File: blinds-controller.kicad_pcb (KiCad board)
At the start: 2 copper layers, 50 x 70 mm, 18 parts, among them J1 Jack-DC, J2 Stepper Motor, J3 DC Check, J4 JTAG, SW1 RESET, U1 MPM3610AGQV-P, U2 ESP32-S2-WROOM, U3 ULN2003A

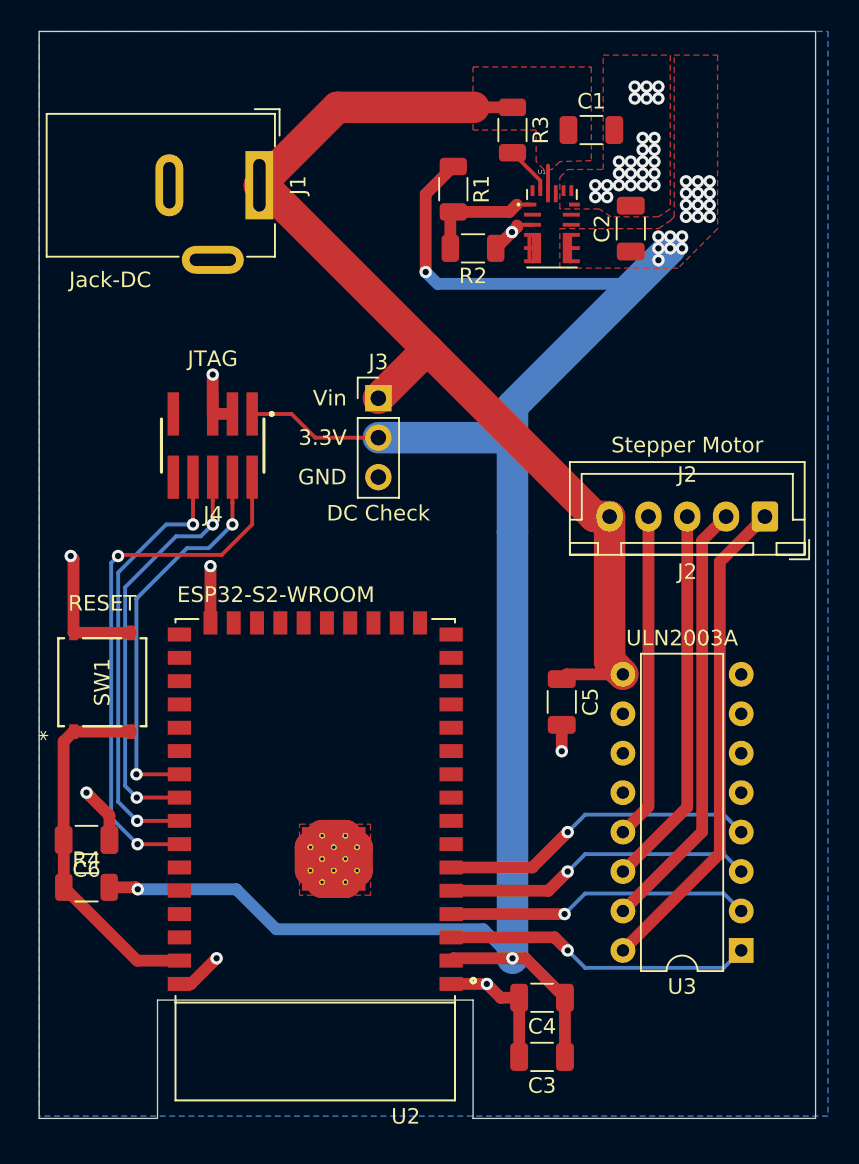
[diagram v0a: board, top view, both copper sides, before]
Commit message: Added PCB holes
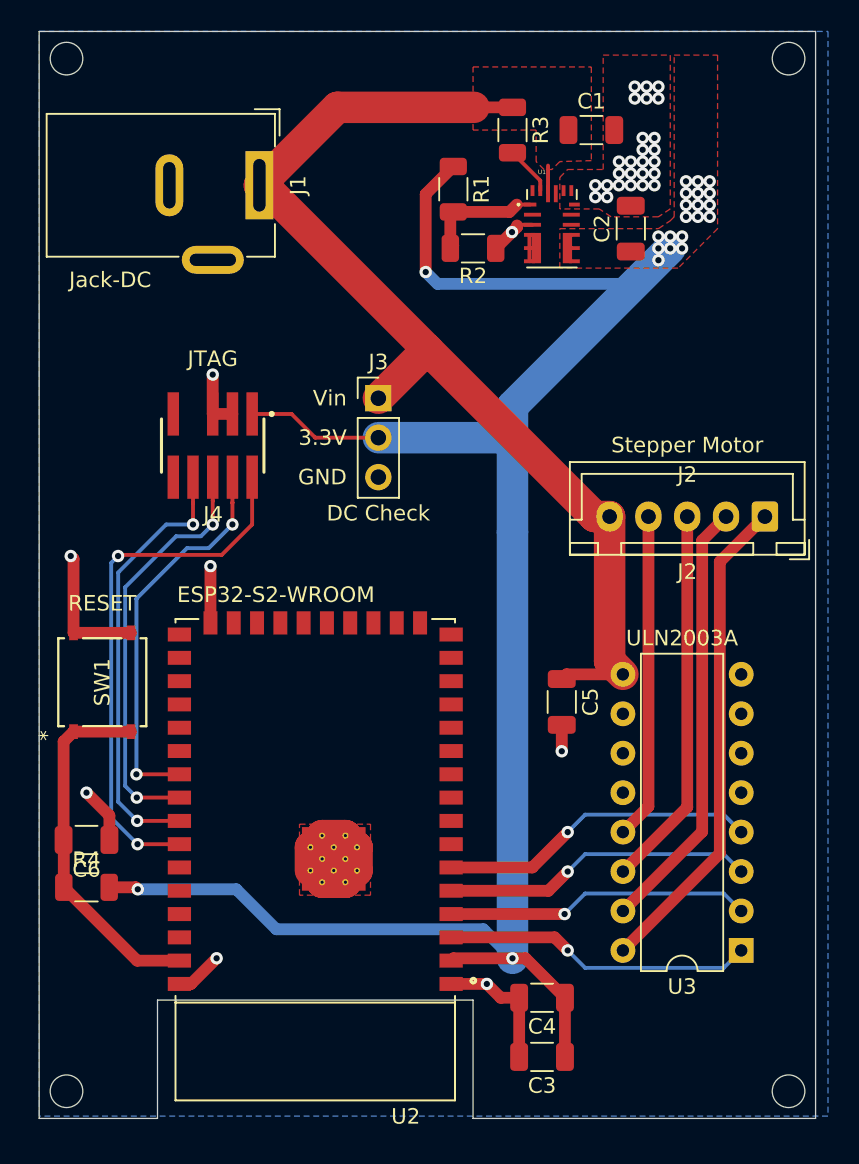
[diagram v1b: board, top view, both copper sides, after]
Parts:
- added REF**: MountingHole_2.1mm, MountingHole:MountingHole_2.1mm, F.Cu at (55.1, 87.3)
- added REF**: MountingHole_2.1mm, MountingHole:MountingHole_2.1mm, F.Cu at (101.6, 87.3)
- added REF**: MountingHole_2.1mm, MountingHole:MountingHole_2.1mm, F.Cu at (101.6, 20.8)
- added REF**: MountingHole_2.1mm, MountingHole:MountingHole_2.1mm, F.Cu at (55.1, 20.8)
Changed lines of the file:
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@@
   (general
     (thickness 1.6)
-    (drawings 19)
+    (drawings 22)
     (tracks 239)
     (zones 0)
-    (modules 18)
+    (modules 22)
     (nets 20)
   )
@@
     (mod_text_size 1 1)
     (mod_text_width 0.15)
-    (pad_size 2.2 2.2)
-    (pad_drill 2.2)
+    (pad_size 2.1 2.1)
+    (pad_drill 2.1)
     (pad_to_mask_clearance 0)
     (aux_axis_origin 0 0)
@@
     (add_net Stepper.D)
   )
+  (module MountingHole:MountingHole_2.1mm (layer F.Cu)
+    (at 55.1 87.3)
+    (descr "Mounting Hole 2.1mm, no annular")
+    (tags "mounting hole 2.1mm no annular")
+    (attr virtual)
+    (fp_text reference REF** (at 0 -3.2) (layer F.SilkS) hide
+      (effects (font (size 1 1) (thickness 0.15)))
+    )
+    (fp_text value MountingHole_2.1mm (at 0 3.2) (layer F.Fab) hide
+      (effects (font (size 1 1) (thickness 0.15)))
+    )
+    (fp_circle (center 0 0) (end 2.1 0) (layer Cmts.User) (width 0.15))
+    (fp_circle (center 0 0) (end 2.35 0) (layer F.CrtYd) (width 0.05))
+    (fp_text user %R (at 0.3 0) (layer F.Fab) hide
+      (effects (font (size 1 1) (thickness 0.15)))
+    )
+    (pad "" np_thru_hole circle (at 0 0) (size 2.1 2.1) (drill 2.1) (layers *.Cu *.Mask))
+  )
+  (module MountingHole:MountingHole_2.1mm (layer F.Cu)
+    (at 101.6 87.3)
+    (descr "Mounting Hole 2.1mm, no annular")
+    (tags "mounting hole 2.1mm no annular")
+    (attr virtual)
+    (fp_text reference REF** (at 0 -3.2) (layer F.SilkS) hide
+      (effects (font (size 1 1) (thickness 0.15)))
+    )
+    (fp_text value MountingHole_2.1mm (at 0 3.2) (layer F.Fab) hide
+      (effects (font (size 1 1) (thickness 0.15)))
+    )
+    (fp_circle (center 0 0) (end 2.1 0) (layer Cmts.User) (width 0.15))
+    (fp_circle (center 0 0) (end 2.35 0) (layer F.CrtYd) (width 0.05))
+    (fp_text user %R (at 0.3 0) (layer F.Fab) hide
+      (effects (font (size 1 1) (thickness 0.15)))
+    )
+    (pad "" np_thru_hole circle (at 0 0) (size 2.1 2.1) (drill 2.1) (layers *.Cu *.Mask))
+  )
+  (module MountingHole:MountingHole_2.1mm (layer F.Cu)
+    (at 101.58 20.79)
+    (descr "Mounting Hole 2.1mm, no annular")
+    (tags "mounting hole 2.1mm no annular")
+    (attr virtual)
+    (fp_text reference REF** (at 0 -3.2) (layer F.SilkS) hide
+      (effects (font (size 1 1) (thickness 0.15)))
+    )
+    (fp_text value MountingHole_2.1mm (at 0 3.2) (layer F.Fab) hide
+      (effects (font (size 1 1) (thickness 0.15)))
+    )
+    (fp_circle (center 0 0) (end 2.1 0) (layer Cmts.User) (width 0.15))
+    (fp_circle (center 0 0) (end 2.35 0) (layer F.CrtYd) (width 0.05))
+    (fp_text user %R (at 0.3 0) (layer F.Fab) hide
+      (effects (font (size 1 1) (thickness 0.15)))
+    )
+    (pad "" np_thru_hole circle (at 0.02 0.01) (size 2.1 2.1) (drill 2.1) (layers *.Cu *.Mask))
+  )
+  (module MountingHole:MountingHole_2.1mm locked (layer F.Cu)
+    (at 55.1 20.8)
+    (descr "Mounting Hole 2.1mm, no annular")
+    (tags "mounting hole 2.1mm no annular")
+    (attr virtual)
+    (fp_text reference REF** (at 0 -3.2) (layer F.SilkS) hide
+      (effects (font (size 1 1) (thickness 0.15)))
+    )
+    (fp_text value MountingHole_2.1mm (at 0 3.2) (layer F.Fab) hide
+      (effects (font (size 1 1) (thickness 0.15)))
+    )
+    (fp_text user %R (at 0.3 0) (layer F.Fab) hide
+      (effects (font (size 1 1) (thickness 0.15)))
+    )
+    (fp_circle (center 0 0) (end 2.1 0) (layer Cmts.User) (width 0.15))
+    (fp_circle (center 0 0) (end 2.35 0) (layer F.CrtYd) (width 0.05))
+    (pad "" np_thru_hole circle (at 0 0) (size 2.1 2.1) (drill 2.1) (layers *.Cu *.Mask))
+  )
   (module Resistor_SMD:R_1206_3216Metric (layer F.Cu)
     (at 56.388 74.168 180)
@@
       (net 2 GND))
   )
-  (dimension 1.74 (width 0.12) (layer Dwgs.User)
-    (gr_text "1.740 mm" (at 102.47 14.13) (layer Dwgs.User)
-      (effects (font (size 1 1) (thickness 0.15)))
-    )
-    (feature1 (pts (xy 101.6 19.05) (xy 101.6 14.813579)))
+  (dimension 1.75 (width 0.12) (layer Dwgs.User)
+    (gr_text "1.750 mm" (at 102.475 92.75) (layer Dwgs.User)
+      (effects (font (size 1 1) (thickness 0.15)))
+    )
+    (feature1 (pts (xy 101.6 89.05) (xy 101.6 92.066421)))
+    (feature2 (pts (xy 103.35 89.05) (xy 103.35 92.066421)))
+    (crossbar (pts (xy 103.35 91.48) (xy 101.6 91.48)))
+    (arrow1a (pts (xy 101.6 91.48) (xy 102.726504 90.893579)))
+    (arrow1b (pts (xy 101.6 91.48) (xy 102.726504 92.066421)))
+    (arrow2a (pts (xy 103.35 91.48) (xy 102.223496 90.893579)))
+    (arrow2b (pts (xy 103.35 91.48) (xy 102.223496 92.066421)))
+  )
+  (dimension 1.75 (width 0.12) (layer Dwgs.User)
+    (gr_text "1.750 mm" (at 106.66 88.175 90) (layer Dwgs.User)
+      (effects (font (size 1 1) (thickness 0.15)))
+    )
+    (feature1 (pts (xy 103.35 87.3) (xy 105.976421 87.3)))
+    (feature2 (pts (xy 103.35 89.05) (xy 105.976421 89.05)))
+    (crossbar (pts (xy 105.39 89.05) (xy 105.39 87.3)))
+    (arrow1a (pts (xy 105.39 87.3) (xy 105.976421 88.426504)))
+    (arrow1b (pts (xy 105.39 87.3) (xy 104.803579 88.426504)))
+    (arrow2a (pts (xy 105.39 89.05) (xy 105.976421 87.923496)))
+    (arrow2b (pts (xy 105.39 89.05) (xy 104.803579 87.923496)))
+  )
+  (dimension 1.75 (width 0.12) (layer Dwgs.User)
+    (gr_text "1.750 mm" (at 106.03 19.925 270) (layer Dwgs.User)
+      (effects (font (size 1 1) (thickness 0.15)))
+    )
+    (feature1 (pts (xy 103.34 20.8) (xy 105.346421 20.8)))
+    (feature2 (pts (xy 103.34 19.05) (xy 105.346421 19.05)))
+    (crossbar (pts (xy 104.76 19.05) (xy 104.76 20.8)))
+    (arrow1a (pts (xy 104.76 20.8) (xy 104.173579 19.673496)))
+    (arrow1b (pts (xy 104.76 20.8) (xy 105.346421 19.673496)))
+    (arrow2a (pts (xy 104.76 19.05) (xy 104.173579 20.176504)))
+    (arrow2b (pts (xy 104.76 19.05) (xy 105.346421 20.176504)))
+  )
+  (dimension 1.75 (width 0.12) (layer Dwgs.User)
+    (gr_text "1.750 mm" (at 102.465 14.13) (layer Dwgs.User)
+      (effects (font (size 1 1) (thickness 0.15)))
+    )
+    (feature1 (pts (xy 101.59 19.05) (xy 101.59 14.813579)))
     (feature2 (pts (xy 103.34 19.05) (xy 103.34 14.813579)))
-    (crossbar (pts (xy 103.34 15.4) (xy 101.6 15.4)))
-    (arrow1a (pts (xy 101.6 15.4) (xy 102.726504 14.813579)))
-    (arrow1b (pts (xy 101.6 15.4) (xy 102.726504 15.986421)))
+    (crossbar (pts (xy 103.34 15.4) (xy 101.59 15.4)))
+    (arrow1a (pts (xy 101.59 15.4) (xy 102.716504 14.813579)))
+    (arrow1b (pts (xy 101.59 15.4) (xy 102.716504 15.986421)))
     (arrow2a (pts (xy 103.34 15.4) (xy 102.213496 14.813579)))
     (arrow2b (pts (xy 103.34 15.4) (xy 102.213496 15.986421)))
@@
     (arrow2b (pts (xy 50.440952 19.066566) (xy 51.0338 20.1897)))
   )
-  (dimension 1.76 (width 0.12) (layer Dwgs.User)
-    (gr_text "1.760 mm" (at 54.22 14.08) (layer Dwgs.User)
-      (effects (font (size 1 1) (thickness 0.15)))
-    )
-    (feature1 (pts (xy 55.1 19.05) (xy 55.1 14.763579)))
+  (dimension 1.75 (width 0.12) (layer Dwgs.User)
+    (gr_text "1.750 mm" (at 54.215 14.08) (layer Dwgs.User)
+      (effects (font (size 1 1) (thickness 0.15)))
+    )
+    (feature1 (pts (xy 55.09 19.05) (xy 55.09 14.763579)))
     (feature2 (pts (xy 53.34 19.05) (xy 53.34 14.763579)))
-    (crossbar (pts (xy 53.34 15.35) (xy 55.1 15.35)))
-    (arrow1a (pts (xy 55.1 15.35) (xy 53.973496 15.936421)))
-    (arrow1b (pts (xy 55.1 15.35) (xy 53.973496 14.763579)))
+    (crossbar (pts (xy 53.34 15.35) (xy 55.09 15.35)))
+    (arrow1a (pts (xy 55.09 15.35) (xy 53.963496 15.936421)))
+    (arrow1b (pts (xy 55.09 15.35) (xy 53.963496 14.763579)))
     (arrow2a (pts (xy 53.34 15.35) (xy 54.466504 15.936421)))
     (arrow2b (pts (xy 53.34 15.35) (xy 54.466504 14.763579)))
